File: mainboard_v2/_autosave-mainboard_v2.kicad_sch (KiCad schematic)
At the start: 66 parts, among them J1 Servo, J2 ISP Header, J4 HCI Board Conn., J5 Power, J6 Release Button, Q1 BSS138, SW1 SW_Push, U1 ATmega328P-A, U2 TCA9548APWR, U3 RV-3028-C7, U4 EE-SX1140, U7 APX803SR

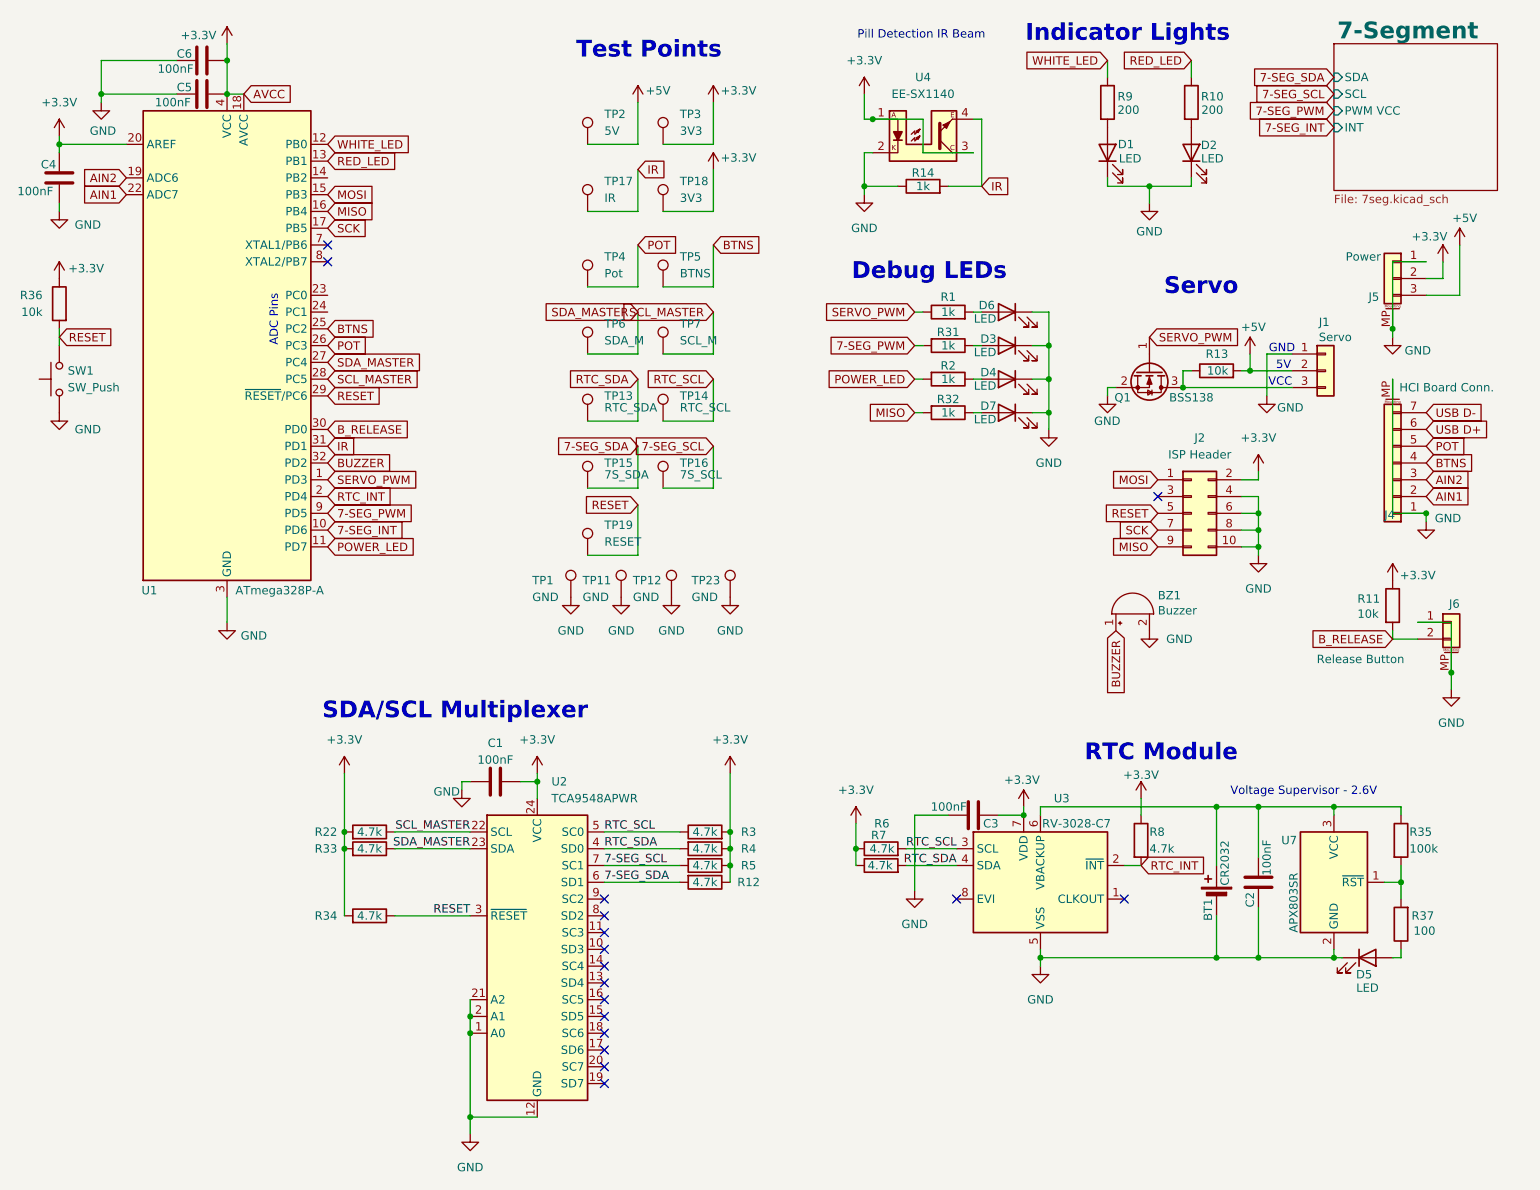
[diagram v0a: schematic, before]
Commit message: updated MCU from RP2040 to ATmega328p
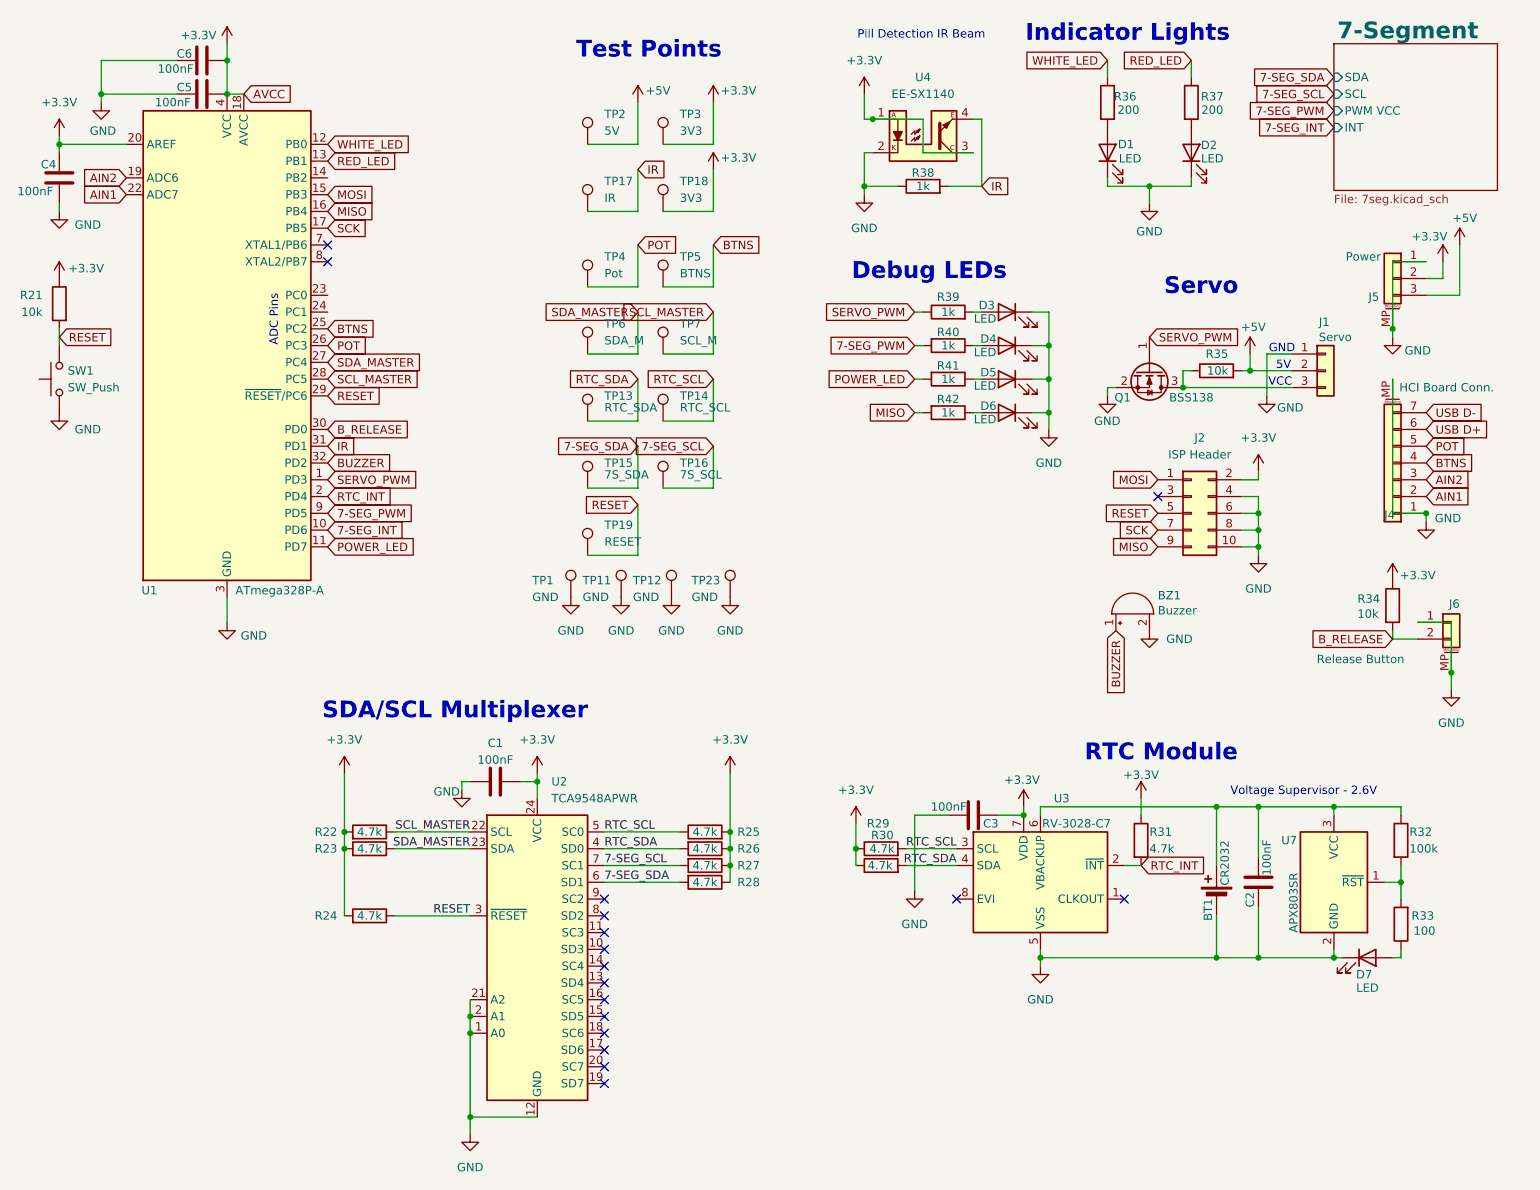
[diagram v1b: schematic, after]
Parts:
- renumbered D6 to D3, D3 to D4, D4 to D5, D7 to D6, D5 to D7, R36 to R21, R33 to R23, R34 to R24, R3 to R25, R4 to R26, R5 to R27, R12 to R28, R6 to R29, R7 to R30, R8 to R31, R35 to R32, R37 to R33, R11 to R34, R13 to R35, R9 to R36, R10 to R37, R14 to R38, R1 to R39, R31 to R40, R2 to R41, R32 to R42
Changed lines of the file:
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@@
 		(on_board yes)
 		(dnp no)
-		(property "Reference" "R35"
+		(property "Reference" "R32"
 			(at 269.24 137.16 0)
 			(effects
@@
 			(project "mainboard_v2"
 				(path "/57f2b6ac-3611-4b16-b8a1-8e91b00e0208"
-					(reference "R35")
+					(reference "R32")
 					(unit 1)
 				)
@@
 		(on_board yes)
 		(dnp no)
-		(property "Reference" "R32"
+		(property "Reference" "R42"
 			(at 199.39 71.628 90)
 			(effects
@@
 			(project "mainboard_v2"
 				(path "/57f2b6ac-3611-4b16-b8a1-8e91b00e0208"
-					(reference "R32")
+					(reference "R42")
 					(unit 1)
 				)
@@
 		(on_board yes)
 		(dnp no)
-		(property "Reference" "R1"
+		(property "Reference" "R39"
 			(at 199.39 56.134 90)
 			(effects
@@
 			(project "mainboard_v2"
 				(path "/57f2b6ac-3611-4b16-b8a1-8e91b00e0208"
-					(reference "R1")
+					(reference "R39")
 					(unit 1)
 				)
@@
 		(on_board yes)
 		(dnp no)
-		(property "Reference" "D7"
+		(property "Reference" "D6"
 			(at 205.486 72.644 0)
 			(effects
@@
 			(project "mainboard_v2"
 				(path "/57f2b6ac-3611-4b16-b8a1-8e91b00e0208"
-					(reference "D7")
+					(reference "D6")
 					(unit 1)
 				)
@@
 		(on_board yes)
 		(dnp no)
-		(property "Reference" "R31"
+		(property "Reference" "R40"
 			(at 199.39 61.468 90)
 			(effects
@@
 			(project "mainboard_v2"
 				(path "/57f2b6ac-3611-4b16-b8a1-8e91b00e0208"
-					(reference "R31")
+					(reference "R40")
 					(unit 1)
 				)
@@
 		(on_board yes)
 		(dnp no)
-		(property "Reference" "D3"
+		(property "Reference" "D4"
 			(at 205.486 62.484 0)
 			(effects
@@
 			(project "mainboard_v2"
 				(path "/57f2b6ac-3611-4b16-b8a1-8e91b00e0208"
-					(reference "D3")
+					(reference "D4")
 					(unit 1)
 				)
@@
 		(on_board yes)
 		(dnp no)
-		(property "Reference" "R37"
+		(property "Reference" "R33"
 			(at 271.272 149.86 0)
 			(effects
@@
 			(project "mainboard_v2"
 				(path "/57f2b6ac-3611-4b16-b8a1-8e91b00e0208"
-					(reference "R37")
+					(reference "R33")
 					(unit 1)
 				)
@@
 		(on_board yes)
 		(dnp no)
-		(property "Reference" "R6"
+		(property "Reference" "R29"
 			(at 190.5 135.89 90)
 			(effects
@@
 			(project "pill_dispenser"
 				(path "/57f2b6ac-3611-4b16-b8a1-8e91b00e0208"
-					(reference "R6")
+					(reference "R29")
 					(unit 1)
 				)
@@
 		(on_board yes)
 		(dnp no)
-		(property "Reference" "R8"
+		(property "Reference" "R31"
 			(at 229.87 137.16 0)
 			(effects
@@
 			(project "pill_dispenser"
 				(path "/57f2b6ac-3611-4b16-b8a1-8e91b00e0208"
-					(reference "R8")
+					(reference "R31")
 					(unit 1)
 				)
@@
 		(on_board yes)
 		(dnp no)
-		(property "Reference" "R36"
+		(property "Reference" "R21"
 			(at 62.23 55.8799 0)
 			(effects
@@
 			(project ""
 				(path "/57f2b6ac-3611-4b16-b8a1-8e91b00e0208"
-					(reference "R36")
+					(reference "R21")
 					(unit 1)
 				)
@@
 		(on_board yes)
 		(dnp no)
-		(property "Reference" "R14"
+		(property "Reference" "R38"
 			(at 195.58 37.338 90)
 			(effects
@@
 			(project ""
 				(path "/57f2b6ac-3611-4b16-b8a1-8e91b00e0208"
-					(reference "R14")
+					(reference "R38")
 					(unit 1)
 				)
@@
 		(on_board yes)
 		(dnp no)
-		(property "Reference" "R5"
+		(property "Reference" "R27"
 			(at 169.164 142.24 90)
 			(effects
@@
 			(project "mainboard_v2"
 				(path "/57f2b6ac-3611-4b16-b8a1-8e91b00e0208"
-					(reference "R5")
+					(reference "R27")
 					(unit 1)
 				)
@@
 		(on_board yes)
 		(dnp no)
-		(property "Reference" "D4"
+		(property "Reference" "D5"
 			(at 205.486 67.564 0)
 			(effects
@@
 			(project "mainboard_v2"
 				(path "/57f2b6ac-3611-4b16-b8a1-8e91b00e0208"
-					(reference "D4")
+					(reference "D5")
 					(unit 1)
 				)
@@
 		(on_board yes)
 		(dnp no)
-		(property "Reference" "R3"
+		(property "Reference" "R25"
 			(at 169.164 137.16 90)
 			(effects
@@
 			(project ""
 				(path "/57f2b6ac-3611-4b16-b8a1-8e91b00e0208"
-					(reference "R3")
+					(reference "R25")
 					(unit 1)
 				)
@@
 		(on_board yes)
 		(dnp no)
-		(property "Reference" "R34"
+		(property "Reference" "R24"
 			(at 105.156 149.86 90)
 			(effects
@@
 			(project "mainboard_v2"
 				(path "/57f2b6ac-3611-4b16-b8a1-8e91b00e0208"
-					(reference "R34")
+					(reference "R24")
 					(unit 1)
 				)
@@
 		(on_board yes)
 		(dnp no)
-		(property "Reference" "R13"
+		(property "Reference" "R35"
 			(at 241.808 64.77 90)
 			(effects
@@
 			(project "pill_dispenser"
 				(path "/57f2b6ac-3611-4b16-b8a1-8e91b00e0208"
-					(reference "R13")
+					(reference "R35")
 					(unit 1)
 				)
@@
 		(on_board yes)
 		(dnp no)
-		(property "Reference" "D6"
+		(property "Reference" "D3"
 			(at 205.232 57.404 0)
 			(effects
@@
 			(project "mainboard_v2"
 				(path "/57f2b6ac-3611-4b16-b8a1-8e91b00e0208"
-					(reference "D6")
+					(reference "D3")
 					(unit 1)
 				)
@@
 		(on_board yes)
 		(dnp no)
-		(property "Reference" "D5"
+		(property "Reference" "D7"
 			(at 262.382 158.75 0)
 			(effects
@@
 			(project ""
 				(path "/57f2b6ac-3611-4b16-b8a1-8e91b00e0208"
-					(reference "D5")
+					(reference "D7")
 					(unit 1)
 				)
@@
 		(on_board yes)
 		(dnp no)
-		(property "Reference" "R33"
+		(property "Reference" "R23"
 			(at 105.156 139.7 90)
 			(effects
@@
 			(project "mainboard_v2"
 				(path "/57f2b6ac-3611-4b16-b8a1-8e91b00e0208"
-					(reference "R33")
+					(reference "R23")
 					(unit 1)
 				)
@@
 		(on_board yes)
 		(dnp no)
-		(property "Reference" "R2"
+		(property "Reference" "R41"
 			(at 199.39 66.548 90)
 			(effects
@@
 			(project "mainboard_v2"
 				(path "/57f2b6ac-3611-4b16-b8a1-8e91b00e0208"
-					(reference "R2")
+					(reference "R41")
 					(unit 1)
 				)
@@
 		(on_board yes)
 		(dnp no)
-		(property "Reference" "R7"
+		(property "Reference" "R30"
 			(at 187.706 137.668 90)
 			(effects
@@
 			(project "pill_dispenser"
 				(path "/57f2b6ac-3611-4b16-b8a1-8e91b00e0208"
-					(reference "R7")
+					(reference "R30")
 					(unit 1)
 				)
@@
 		(on_board yes)
 		(dnp no)
-		(property "Reference" "R4"
+		(property "Reference" "R26"
 			(at 169.164 139.7 90)
 			(effects
@@
 			(project ""
 				(path "/57f2b6ac-3611-4b16-b8a1-8e91b00e0208"
-					(reference "R4")
+					(reference "R26")
 					(unit 1)
 				)
@@
 		(on_board yes)
 		(dnp no)
-		(property "Reference" "R10"
+		(property "Reference" "R37"
 			(at 239.395 25.781 0)
 			(effects
@@
 			(project "pill_dispenser"
 				(path "/57f2b6ac-3611-4b16-b8a1-8e91b00e0208"
-					(reference "R10")
+					(reference "R37")
 					(unit 1)
 				)
@@
 		(on_board yes)
 		(dnp no)
-		(property "Reference" "R11"
+		(property "Reference" "R34"
 			(at 261.366 101.854 0)
 			(effects
@@
 			(project "pill_dispenser"
 				(path "/57f2b6ac-3611-4b16-b8a1-8e91b00e0208"
-					(reference "R11")
+					(reference "R34")
 					(unit 1)
 				)
@@
 		(on_board yes)
 		(dnp no)
-		(property "Reference" "R9"
+		(property "Reference" "R36"
 			(at 226.187 25.781 0)
 			(effects
@@
 			(project ""
 				(path "/57f2b6ac-3611-4b16-b8a1-8e91b00e0208"
-					(reference "R9")
+					(reference "R36")
 					(unit 1)
 				)
@@
 		(on_board yes)
 		(dnp no)
-		(property "Reference" "R12"
+		(property "Reference" "R28"
 			(at 169.164 144.78 90)
 			(effects
@@
 			(project "mainboard_v2"
 				(path "/57f2b6ac-3611-4b16-b8a1-8e91b00e0208"
-					(reference "R12")
+					(reference "R28")
 					(unit 1)
 				)
